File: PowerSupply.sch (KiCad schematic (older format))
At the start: 13 parts, among them IC1 TPS61240IDRVRQ1, U1 LM27762

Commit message: selecting actual components
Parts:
- removed C1: 4.7u/10V, symbol Device:C
- removed C2, C5, C6: 2.2u/16V, symbol Device:C
- removed C4: C, symbol Device:C
- removed IC1: TPS61240IDRVRQ1, SamacSys_PCB_Library:SON65P200X200X80-7N, symbol BalancedAudioBox:TPS61240IDRVRQ1
- removed L1: 1u/1.3A, symbol Device:L
- added C?: 100p, Capacitor_SMD:C_0201_0603Metric, symbol Device:C
- added C? (x5): 10u/25V, Resistor_SMD:R_0805_2012Metric, symbol Device:C
- added IC?: TPS61252DSGT, SON50P200X200X80-9N, symbol BalancedAudioBox:TPS61252DSGT
- added L?: 1.5u, symbol Device:L
- added R?: 634k, Resistor_SMD:R_0603_1608Metric, symbol Device:R
- added R?: 180k, Resistor_SMD:R_0603_1608Metric, symbol Device:R
- added R?: 47k, Resistor_SMD:R_0402_1005Metric, symbol Device:R
- R1, R2: value R -> 1.58M
- R3, R4: value R -> 499k
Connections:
- net labels added: VIN
- wire segments 61 -> 78
- no-connect marks 0 -> 1
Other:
- note added: "2.5V-5V to 5.40V @ 0.1A"
- note added: "5.3V-5.5V to 2x5V @ 75mA"
- note added: "R_inp_lim=10k/I_inp_lim"
- note added: "minimum 2.2uF on output; but we already have 2x10u on load.\nmin. load: 5mA"
- moved on the sheet: R1, R2, R3, R4

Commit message: work
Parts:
- added C21, C22: 4.7u, Capacitor_SMD:C_0805_2012Metric, symbol Device:C
- added PS1: DPU01L-15, SamacSys_PCB_Library:DPU01L15, symbol BalancedAudioBox:DPU01L-15
- C1, C20, C4, C5, C6: renamed from C?; footprint Resistor_SMD:R_0805_2012Metric -> Capacitor_SMD:C_0805_2012Metric
- C3: footprint (none) -> Capacitor_SMD:C_0805_2012Metric
- IC1: renamed from IC?; footprint SON50P200X200X80-9N -> SamacSys_PCB_Library:SON50P200X200X80-9N
- gave numbers to parts that had none: 5
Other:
- note added: "Alternative power supply"
- note added: "minimum 2.2uF on output; at 20uF we already have a lot of overshoot\nmin. load: 5mA"
- note removed: "minimum 2.2uF on output; but we already have 2x10u on load.\nmin. load: 5mA"
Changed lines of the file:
@@
 F 0 "C3" H 6765 4146 50  0000 L CNN
 F 1 "4.7u" H 6765 4055 50  0000 L CNN
-F 2 "" H 6688 3950 50  0001 C CNN
+F 2 "Capacitor_SMD:C_0805_2012Metric" H 6688 3950 50  0001 C CNN
 F 3 "~" H 6650 4100 50  0001 C CNN
 	1    6650 4100
@@
 	6850 3700 6850 3400
 $Comp
-L BalancedAudioBox:TPS61252DSGT IC?
+L BalancedAudioBox:TPS61252DSGT IC1
 U 1 1 5D3E64AD
 P 3700 3300
-F 0 "IC?" H 4300 3565 50  0000 C CNN
+F 0 "IC1" H 4300 3565 50  0000 C CNN
 F 1 "TPS61252DSGT" H 4300 3474 50  0000 C CNN
-F 2 "SON50P200X200X80-9N" H 4750 3400 50  0001 L CNN
+F 2 "SamacSys_PCB_Library:SON50P200X200X80-9N" H 4750 3400 50  0001 L CNN
 F 3 "http://www.ti.com/lit/ds/symlink/tps61252.pdf" H 4750 3300 50  0001 L CNN
 F 4 "TPS61252DSGT, DC-DC Converter, 1500mA Adjustable, 3  6.5 V, Step Up, 3.25 MHz, 8-Pin SON W" H 4750 3200 50  0001 L CNN "Description"
@@
 $EndComp
 $Comp
-L Device:C C?
+L Device:C C2
 U 1 1 5D3E7B90
 P 4250 3600
-F 0 "C?" H 4365 3646 50  0000 L CNN
+F 0 "C2" H 4365 3646 50  0000 L CNN
 F 1 "100p" H 4365 3555 50  0000 L CNN
 F 2 "Capacitor_SMD:C_0201_0603Metric" H 4288 3450 50  0001 C CNN
@@
 $EndComp
 $Comp
-L Device:R R?
+L Device:R R14
 U 1 1 5D3E88D9
 P 4650 3600
-F 0 "R?" H 4720 3646 50  0000 L CNN
+F 0 "R14" H 4720 3646 50  0000 L CNN
 F 1 "634k" H 4720 3555 50  0000 L CNN
 F 2 "Resistor_SMD:R_0603_1608Metric" V 4580 3600 50  0001 C CNN
@@
 $EndComp
 $Comp
-L Device:R R?
+L Device:R R15
 U 1 1 5D3E95C9
 P 4650 4100
-F 0 "R?" H 4720 4146 50  0000 L CNN
+F 0 "R15" H 4720 4146 50  0000 L CNN
 F 1 "180k" H 4720 4055 50  0000 L CNN
 F 2 "Resistor_SMD:R_0603_1608Metric" V 4580 4100 50  0001 C CNN
@@
 NoConn ~ 2500 3600
 $Comp
-L Device:L L?
+L Device:L L1
 U 1 1 5D3EB043
 P 2200 3400
-F 0 "L?" V 2000 3400 50  0000 C CNN
+F 0 "L1" V 2000 3400 50  0000 C CNN
 F 1 "1.5u" V 2100 3400 50  0000 C CNN
 F 2 "" H 2200 3400 50  0001 C CNN
@@
 Connection ~ 4650 3400
 $Comp
-L power:GND #PWR?
+L power:GND #PWR052
 U 1 1 5D3FC530
 P 4000 4700
-F 0 "#PWR?" H 4000 4450 50  0001 C CNN
+F 0 "#PWR052" H 4000 4450 50  0001 C CNN
 F 1 "GND" H 4005 4527 50  0000 C CNN
 F 2 "" H 4000 4700 50  0001 C CNN
@@
 $EndComp
 $Comp
-L Device:R R?
+L Device:R R13
 U 1 1 5D3FE154
 P 3700 4000
-F 0 "R?" H 3630 3954 50  0000 R CNN
+F 0 "R13" H 3630 3954 50  0000 R CNN
 F 1 "47k" H 3630 4045 50  0000 R CNN
 F 2 "Resistor_SMD:R_0402_1005Metric" V 3630 4000 50  0001 C CNN
@@
 	3700 3850 3700 3600
 $Comp
-L power:GND #PWR?
+L power:GND #PWR051
 U 1 1 5D40A0B6
 P 3700 4700
-F 0 "#PWR?" H 3700 4450 50  0001 C CNN
+F 0 "#PWR051" H 3700 4450 50  0001 C CNN
 F 1 "GND" H 3705 4527 50  0000 C CNN
 F 2 "" H 3700 4700 50  0001 C CNN
@@
 2.5V-5V to 5.40V @ 0.1A
 $Comp
-L Device:C C?
+L Device:C C1
 U 1 1 5D41488C
 P 1700 3950
-F 0 "C?" H 1815 3996 50  0000 L CNN
+F 0 "C1" H 1815 3996 50  0000 L CNN
 F 1 "10u/25V" H 1815 3905 50  0000 L CNN
-F 2 "Resistor_SMD:R_0805_2012Metric" H 1738 3800 50  0001 C CNN
+F 2 "Capacitor_SMD:C_0805_2012Metric" H 1738 3800 50  0001 C CNN
 F 3 "~" H 1700 3950 50  0001 C CNN
 F 4 "TMK212BBJ106MG-T" H 1700 3950 50  0001 C CNN "PN"
@@
 $EndComp
 $Comp
-L Device:C C?
+L Device:C C4
 U 1 1 5D4150B1
 P 4950 3900
-F 0 "C?" H 5065 3946 50  0000 L CNN
+F 0 "C4" H 5065 3946 50  0000 L CNN
 F 1 "10u/25V" H 5065 3855 50  0000 L CNN
-F 2 "Resistor_SMD:R_0805_2012Metric" H 4988 3750 50  0001 C CNN
+F 2 "Capacitor_SMD:C_0805_2012Metric" H 4988 3750 50  0001 C CNN
 F 3 "~" H 4950 3900 50  0001 C CNN
 F 4 "TMK212BBJ106MG-T" H 4950 3900 50  0001 C CNN "PN"
@@
 $EndComp
 $Comp
-L power:GND #PWR?
+L power:GND #PWR053
 U 1 1 5D4185FE
 P 5500 4700
-F 0 "#PWR?" H 5500 4450 50  0001 C CNN
+F 0 "#PWR053" H 5500 4450 50  0001 C CNN
 F 1 "GND" H 5505 4527 50  0000 C CNN
 F 2 "" H 5500 4700 50  0001 C CNN
@@
 $EndComp
 $Comp
-L Device:C C?
+L Device:C C5
 U 1 1 5D418607
 P 5500 3900
-F 0 "C?" H 5615 3946 50  0000 L CNN
+F 0 "C5" H 5615 3946 50  0000 L CNN
 F 1 "10u/25V" H 5615 3855 50  0000 L CNN
-F 2 "Resistor_SMD:R_0805_2012Metric" H 5538 3750 50  0001 C CNN
+F 2 "Capacitor_SMD:C_0805_2012Metric" H 5538 3750 50  0001 C CNN
 F 3 "~" H 5500 3900 50  0001 C CNN
 F 4 "TMK212BBJ106MG-T" H 5500 3900 50  0001 C CNN "PN"
@@
 $EndComp
 $Comp
-L power:GND #PWR?
+L power:GND #PWR054
 U 1 1 5D41A9F0
 P 6050 4700
-F 0 "#PWR?" H 6050 4450 50  0001 C CNN
+F 0 "#PWR054" H 6050 4450 50  0001 C CNN
 F 1 "GND" H 6055 4527 50  0000 C CNN
 F 2 "" H 6050 4700 50  0001 C CNN
@@
 $EndComp
 $Comp
-L Device:C C?
+L Device:C C6
 U 1 1 5D41A9F9
 P 6050 3900
-F 0 "C?" H 6165 3946 50  0000 L CNN
+F 0 "C6" H 6165 3946 50  0000 L CNN
 F 1 "10u/25V" H 6165 3855 50  0000 L CNN
-F 2 "Resistor_SMD:R_0805_2012Metric" H 6088 3750 50  0001 C CNN
+F 2 "Capacitor_SMD:C_0805_2012Metric" H 6088 3750 50  0001 C CNN
 F 3 "~" H 6050 3900 50  0001 C CNN
 F 4 "TMK212BBJ106MG-T" H 6050 3900 50  0001 C CNN "PN"
@@
 	1700 3300 1900 3300
 $Comp
-L power:GND #PWR?
+L power:GND #PWR050
 U 1 1 5D43E999
 P 1700 4700
-F 0 "#PWR?" H 1700 4450 50  0001 C CNN
+F 0 "#PWR050" H 1700 4450 50  0001 C CNN
 F 1 "GND" H 1705 4527 50  0000 C CNN
 F 2 "" H 1700 4700 50  0001 C CNN
@@
 Connection ~ 10550 4350
 $Comp
-L Device:C C?
+L Device:C C20
 U 1 1 5D45C51D
 P 8100 4500
-F 0 "C?" H 8215 4546 50  0000 L CNN
+F 0 "C20" H 8215 4546 50  0000 L CNN
 F 1 "10u/25V" H 8215 4455 50  0000 L CNN
-F 2 "Resistor_SMD:R_0805_2012Metric" H 8138 4350 50  0001 C CNN
+F 2 "Capacitor_SMD:C_0805_2012Metric" H 8138 4350 50  0001 C CNN
 F 3 "~" H 8100 4500 50  0001 C CNN
 F 4 "TMK212BBJ106MG-T" H 8100 4500 50  0001 C CNN "PN"
@@
 	4000 3300 4000 4700
 Text Notes 8150 5400 0    50   ~ 0
-minimum 2.2uF on output; but we already have 2x10u on load.\nmin. load: 5mA
+minimum 2.2uF on output; at 20uF we already have a lot of overshoot\nmin. load: 5mA
+$Comp
+L BalancedAudioBox:DPU01L-15 PS1
+U 1 1 5D3EF611
+P 4600 1650
+F 0 "PS1" H 5250 1915 50  0000 C CNN
+F 1 "DPU01L-15" H 5250 1824 50  0000 C CNN
+F 2 "SamacSys_PCB_Library:DPU01L15" H 5750 1750 50  0001 L CNN
+F 3 "https://media.digikey.com/pdf/Data%20Sheets/Mean%20Well%20PDF's/SPU01,DUP01_Series_Ds.pdf" H 5750 1650 50  0001 L CNN
+F 4 "Isolated DC/DC Converters 4.5-5.5Vin +/-15Vout +/-33mA SIP6 Unreg" H 5750 1550 50  0001 L CNN "Description"
+F 5 "10.45" H 5750 1450 50  0001 L CNN "Height"
+F 6 "Mean Well" H 5750 1350 50  0001 L CNN "Manufacturer_Name"
+F 7 "DPU01L-15" H 5750 1250 50  0001 L CNN "Manufacturer_Part_Number"
+F 8 "709-DPU01L-15" H 5750 1150 50  0001 L CNN "Mouser Part Number"
+F 9 "https://www.mouser.com/Search/Refine.aspx?Keyword=709-DPU01L-15" H 5750 1050 50  0001 L CNN "Mouser Price/Stock"
+F 10 "" H 5750 950 50  0001 L CNN "RS Part Number"
+F 11 "" H 5750 850 50  0001 L CNN "RS Price/Stock"
+F 12 "71028144" H 5750 750 50  0001 L CNN "Allied_Number"
+F 13 "https://www.alliedelec.com/meanwellusa-dpu01l-15/71028144/" H 5750 650 50  0001 L CNN "Allied Price/Stock"
+	1    4600 1650
+	1    0    0    -1
+$EndComp
+Text Notes 4900 1200 0    50   ~ 0
+Alternative power supply
+$Comp
+L Device:C C21
+U 1 1 5D3F13AC
+P 8650 4500
+F 0 "C21" H 8765 4546 50  0000 L CNN
+F 1 "4.7u" H 8765 4455 50  0000 L CNN
+F 2 "Capacitor_SMD:C_0805_2012Metric" H 8688 4350 50  0001 C CNN
+F 3 "~" H 8650 4500 50  0001 C CNN
+	1    8650 4500
+	1    0    0    -1
+$EndComp
+$Comp
+L Device:C C22
+U 1 1 5D3F1A6F
+P 9300 4500
+F 0 "C22" H 9415 4546 50  0000 L CNN
+F 1 "4.7u" H 9415 4455 50  0000 L CNN
+F 2 "Capacitor_SMD:C_0805_2012Metric" H 9338 4350 50  0001 C CNN
+F 3 "~" H 9300 4500 50  0001 C CNN
+	1    9300 4500
+	1    0    0    -1
+$EndComp
 $EndSCHEMATC

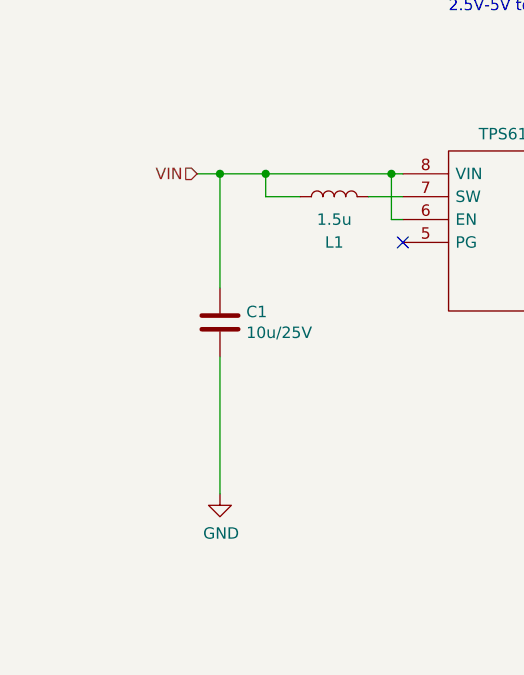
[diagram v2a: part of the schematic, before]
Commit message: TPS61252 done
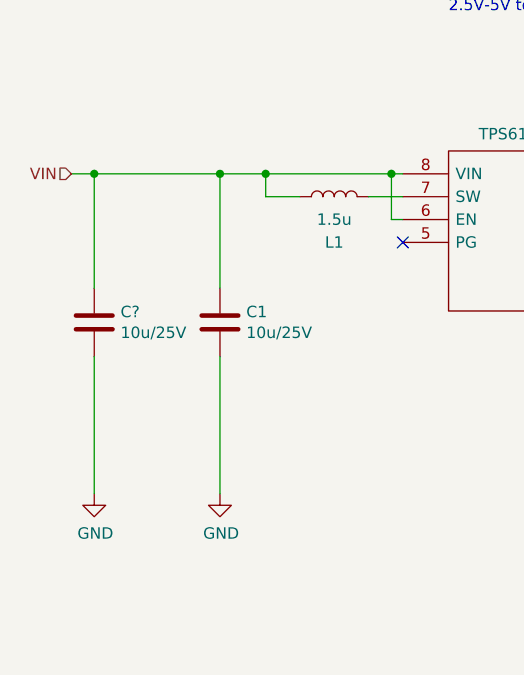
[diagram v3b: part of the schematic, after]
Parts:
- added C?: 10u/25V, Capacitor_SMD:C_0805_2012Metric, symbol Device:C
- C2: footprint Capacitor_SMD:C_0201_0603Metric -> Capacitor_SMD:C_0603_1608Metric
- L1: footprint (none) -> BalancedAudioBox:SRN30151R5Y
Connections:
- net GND: now also C?.2
- net VIN: now also C?.1
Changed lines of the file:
@@
 F 0 "C2" H 4365 3646 50  0000 L CNN
 F 1 "100p" H 4365 3555 50  0000 L CNN
-F 2 "Capacitor_SMD:C_0201_0603Metric" H 4288 3450 50  0001 C CNN
+F 2 "Capacitor_SMD:C_0603_1608Metric" H 4288 3450 50  0001 C CNN
 F 3 "~" H 4250 3600 50  0001 C CNN
 F 4 "GRM1885C2A101JA01D" H 4250 3600 50  0001 C CNN "PN"
@@
 F 0 "L1" V 2000 3400 50  0000 C CNN
 F 1 "1.5u" V 2100 3400 50  0000 C CNN
-F 2 "" H 2200 3400 50  0001 C CNN
+F 2 "BalancedAudioBox:SRN30151R5Y" H 2200 3400 50  0001 C CNN
 F 3 "~" H 2200 3400 50  0001 C CNN
 F 4 "SRN3015-1R5Y" V 2200 3400 50  0001 C CNN "PN"
@@
 Text Notes 3350 5200 0    50   ~ 0
 R_inp_lim=10k/I_inp_lim
-Text HLabel 1600 3300 0    50   Input ~ 0
+Text HLabel 1050 3300 0    50   Input ~ 0
 VIN
-Wire Wire Line
-	1600 3300 1700 3300
 Connection ~ 1900 3300
 Text Notes 2700 2600 0    50   ~ 0
@@
 	1    0    0    -1
 $EndComp
+Wire Wire Line
+	1050 3300 1150 3300
+$Comp
+L Device:C C?
+U 1 1 5D43E98B
+P 1150 3950
+F 0 "C?" H 1265 3996 50  0000 L CNN
+F 1 "10u/25V" H 1265 3905 50  0000 L CNN
+F 2 "Capacitor_SMD:C_0805_2012Metric" H 1188 3800 50  0001 C CNN
+F 3 "~" H 1150 3950 50  0001 C CNN
+F 4 "TMK212BBJ106MG-T" H 1150 3950 50  0001 C CNN "PN"
+	1    1150 3950
+	1    0    0    -1
+$EndComp
+Wire Wire Line
+	1150 3800 1150 3300
+$Comp
+L power:GND #PWR?
+U 1 1 5D43E992
+P 1150 4700
+F 0 "#PWR?" H 1150 4450 50  0001 C CNN
+F 1 "GND" H 1155 4527 50  0000 C CNN
+F 2 "" H 1150 4700 50  0001 C CNN
+F 3 "" H 1150 4700 50  0001 C CNN
+	1    1150 4700
+	1    0    0    -1
+$EndComp
+Wire Wire Line
+	1150 4700 1150 4100
+Connection ~ 1150 3300
+Wire Wire Line
+	1150 3300 1700 3300
 $EndSCHEMATC

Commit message: ps checked
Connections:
- net +5V: now also PS1.6 (+VOUT)
- net -5V: now also PS1.4 (-VOUT)
- net GND: now also PS1.2 (-VIN), PS1.5 (COMMON)
- net VIN: now also PS1.1 (+VIN)
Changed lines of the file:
@@
 Wire Wire Line
 	1150 3300 1700 3300
+$Comp
+L power:+5V #PWR?
+U 1 1 5D43903A
+P 6100 1500
+F 0 "#PWR?" H 6100 1350 50  0001 C CNN
+F 1 "+5V" H 6115 1673 50  0000 C CNN
+F 2 "" H 6100 1500 50  0001 C CNN
+F 3 "" H 6100 1500 50  0001 C CNN
+	1    6100 1500
+	1    0    0    -1
+$EndComp
+$Comp
+L power:-5V #PWR?
+U 1 1 5D4393F5
+P 4500 2000
+F 0 "#PWR?" H 4500 2100 50  0001 C CNN
+F 1 "-5V" H 4515 2173 50  0000 C CNN
+F 2 "" H 4500 2000 50  0001 C CNN
+F 3 "" H 4500 2000 50  0001 C CNN
+	1    4500 2000
+	-1   0    0    1
+$EndComp
+$Comp
+L power:GND #PWR?
+U 1 1 5D439932
+P 5950 2050
+F 0 "#PWR?" H 5950 1800 50  0001 C CNN
+F 1 "GND" H 5955 1877 50  0000 C CNN
+F 2 "" H 5950 2050 50  0001 C CNN
+F 3 "" H 5950 2050 50  0001 C CNN
+	1    5950 2050
+	1    0    0    -1
+$EndComp
+Text Label 1700 3300 0    50   ~ 0
+VIN
+Text Label 4300 1650 0    50   ~ 0
+VIN
+Wire Wire Line
+	4600 1650 4300 1650
+$Comp
+L power:GND #PWR?
+U 1 1 5D43C58F
+P 4100 2000
+F 0 "#PWR?" H 4100 1750 50  0001 C CNN
+F 1 "GND" H 4105 1827 50  0000 C CNN
+F 2 "" H 4100 2000 50  0001 C CNN
+F 3 "" H 4100 2000 50  0001 C CNN
+	1    4100 2000
+	1    0    0    -1
+$EndComp
+Wire Wire Line
+	4100 2000 4100 1750
+Wire Wire Line
+	4100 1750 4600 1750
+Wire Wire Line
+	4600 1850 4500 1850
+Wire Wire Line
+	4500 1850 4500 2000
+Wire Wire Line
+	5900 1750 6100 1750
+Wire Wire Line
+	6100 1750 6100 1500
+Wire Wire Line
+	5950 2050 5950 1650
+Wire Wire Line
+	5950 1650 5900 1650
 $EndSCHEMATC

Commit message: placement complete
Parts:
- added J6: Conn_01x02, Connector_PinSocket_2.54mm:PinSocket_1x02_P2.54mm_Vertical, symbol Connector_Generic:Conn_01x02
- IC1: footprint SamacSys_PCB_Library:SON50P200X200X80-9N -> BalancedAudioBox:SON50P200X200X80-9N
- PS1: footprint SamacSys_PCB_Library:DPU01L15 -> BalancedAudioBox:DPU01L15
- gave numbers to parts that had none: 1
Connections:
- net GND: now also J6.2 (Pin_2)
- net VOUT-5.4V: now reaches C2.1, C4.1, C5.1, C6.1, IC1.2 (VOUT), R14.1, U1.12 (EN+), U1.3 (VIN), U1.8 (EN-)
- net VOUT-5.4V: now also J6.1 (Pin_1)
- net FB: now reaches C2.2, IC1.3 (FB), R14.2, R15.1
- net ILIM: now reaches IC1.4 (ILIM), R13.2
- net FB+: now reaches R1.2, R4.1, U1.2 (FB+)
- net CP: now reaches C20.1, U1.5 (CP)
- net FB-: now reaches R2.2, R3.1, U1.7 (FB-)
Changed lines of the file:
@@
 F 0 "IC1" H 4300 3565 50  0000 C CNN
 F 1 "TPS61252DSGT" H 4300 3474 50  0000 C CNN
-F 2 "SamacSys_PCB_Library:SON50P200X200X80-9N" H 4750 3400 50  0001 L CNN
+F 2 "BalancedAudioBox:SON50P200X200X80-9N" H 4750 3400 50  0001 L CNN
 F 3 "http://www.ti.com/lit/ds/symlink/tps61252.pdf" H 4750 3300 50  0001 L CNN
 F 4 "TPS61252DSGT, DC-DC Converter, 1500mA Adjustable, 3  6.5 V, Step Up, 3.25 MHz, 8-Pin SON W" H 4750 3200 50  0001 L CNN "Description"
@@
 Connection ~ 4950 3400
 Wire Wire Line
-	4950 3400 5500 3400
+	4950 3400 5150 3400
 Wire Wire Line
 	5500 3750 5500 3400
@@
 F 0 "PS1" H 5250 1915 50  0000 C CNN
 F 1 "DPU01L-15" H 5250 1824 50  0000 C CNN
-F 2 "SamacSys_PCB_Library:DPU01L15" H 5750 1750 50  0001 L CNN
+F 2 "BalancedAudioBox:DPU01L15" H 5750 1750 50  0001 L CNN
 F 3 "https://media.digikey.com/pdf/Data%20Sheets/Mean%20Well%20PDF's/SPU01,DUP01_Series_Ds.pdf" H 5750 1650 50  0001 L CNN
 F 4 "Isolated DC/DC Converters 4.5-5.5Vin +/-15Vout +/-33mA SIP6 Unreg" H 5750 1550 50  0001 L CNN "Description"
@@
 	1050 3300 1150 3300
 $Comp
-L Device:C C?
+L Device:C C27
 U 1 1 5D43E98B
 P 1150 3950
-F 0 "C?" H 1265 3996 50  0000 L CNN
+F 0 "C27" H 1265 3996 50  0000 L CNN
 F 1 "10u/25V" H 1265 3905 50  0000 L CNN
 F 2 "Capacitor_SMD:C_0805_2012Metric" H 1188 3800 50  0001 C CNN
@@
 	1150 3800 1150 3300
 $Comp
-L power:GND #PWR?
+L power:GND #PWR072
 U 1 1 5D43E992
 P 1150 4700
-F 0 "#PWR?" H 1150 4450 50  0001 C CNN
+F 0 "#PWR072" H 1150 4450 50  0001 C CNN
 F 1 "GND" H 1155 4527 50  0000 C CNN
 F 2 "" H 1150 4700 50  0001 C CNN
@@
 	1150 3300 1700 3300
 $Comp
-L power:+5V #PWR?
+L power:+5V #PWR076
 U 1 1 5D43903A
 P 6100 1500
-F 0 "#PWR?" H 6100 1350 50  0001 C CNN
+F 0 "#PWR076" H 6100 1350 50  0001 C CNN
 F 1 "+5V" H 6115 1673 50  0000 C CNN
 F 2 "" H 6100 1500 50  0001 C CNN
@@
 $EndComp
 $Comp
-L power:-5V #PWR?
+L power:-5V #PWR074
 U 1 1 5D4393F5
 P 4500 2000
-F 0 "#PWR?" H 4500 2100 50  0001 C CNN
+F 0 "#PWR074" H 4500 2100 50  0001 C CNN
 F 1 "-5V" H 4515 2173 50  0000 C CNN
 F 2 "" H 4500 2000 50  0001 C CNN
@@
 $EndComp
 $Comp
-L power:GND #PWR?
+L power:GND #PWR075
 U 1 1 5D439932
 P 5950 2050
-F 0 "#PWR?" H 5950 1800 50  0001 C CNN
+F 0 "#PWR075" H 5950 1800 50  0001 C CNN
 F 1 "GND" H 5955 1877 50  0000 C CNN
 F 2 "" H 5950 2050 50  0001 C CNN
@@
 	4600 1650 4300 1650
 $Comp
-L power:GND #PWR?
+L power:GND #PWR073
 U 1 1 5D43C58F
 P 4100 2000
-F 0 "#PWR?" H 4100 1750 50  0001 C CNN
+F 0 "#PWR073" H 4100 1750 50  0001 C CNN
 F 1 "GND" H 4105 1827 50  0000 C CNN
 F 2 "" H 4100 2000 50  0001 C CNN
@@
 Wire Wire Line
 	5950 1650 5900 1650
+$Comp
+L Connector_Generic:Conn_01x02 J6
+U 1 1 5D46B0BF
+P 5500 3050
+F 0 "J6" H 5580 3042 50  0000 L CNN
+F 1 "Conn_01x02" H 5580 2951 50  0000 L CNN
+F 2 "Connector_PinSocket_2.54mm:PinSocket_1x02_P2.54mm_Vertical" H 5500 3050 50  0001 C CNN
+F 3 "~" H 5500 3050 50  0001 C CNN
+	1    5500 3050
+	1    0    0    -1
+$EndComp
+$Comp
+L power:GND #PWR077
+U 1 1 5D46C0AE
+P 5300 3150
+F 0 "#PWR077" H 5300 2900 50  0001 C CNN
+F 1 "GND" H 5305 2977 50  0000 C CNN
+F 2 "" H 5300 3150 50  0001 C CNN
+F 3 "" H 5300 3150 50  0001 C CNN
+	1    5300 3150
+	1    0    0    -1
+$EndComp
+Wire Wire Line
+	5300 3050 5150 3050
+Wire Wire Line
+	5150 3050 5150 3400
+Connection ~ 5150 3400
+Wire Wire Line
+	5150 3400 5500 3400
+Text Label 6050 3400 0    50   ~ 0
+VOUT-5.4V
+Text Label 8100 4200 0    50   ~ 0
+CP
+Text Label 8100 4000 0    50   ~ 0
+OUT-
+Text Label 8100 3800 0    50   ~ 0
+FB-
+Text Label 8100 3600 0    50   ~ 0
+FB+
+Text Label 6500 3600 0    50   ~ 0
+PGOOD
+Text Label 3700 3600 0    50   ~ 0
+ILIM
+Text Label 4250 3850 0    50   ~ 0
+FB
 $EndSCHEMATC

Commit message: footprint and 3d improvements
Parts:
- R1, R14, R15, R2, R3, R4: footprint Resistor_SMD:R_0603_1608Metric -> Resistor_SMD:R_0402_1005Metric
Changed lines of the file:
@@
 F 0 "R3" H 9920 4596 50  0000 L CNN
 F 1 "499k" H 9920 4505 50  0000 L CNN
-F 2 "Resistor_SMD:R_0603_1608Metric" V 9780 4550 50  0001 C CNN
+F 2 "Resistor_SMD:R_0402_1005Metric" V 9780 4550 50  0001 C CNN
 F 3 "~" H 9850 4550 50  0001 C CNN
 	1    9850 4550
@@
 F 0 "R2" H 9920 4246 50  0000 L CNN
 F 1 "1.58M" H 9920 4155 50  0000 L CNN
-F 2 "Resistor_SMD:R_0603_1608Metric" V 9780 4200 50  0001 C CNN
+F 2 "Resistor_SMD:R_0402_1005Metric" V 9780 4200 50  0001 C CNN
 F 3 "~" H 9850 4200 50  0001 C CNN
 	1    9850 4200
@@
 F 0 "R4" H 10620 4596 50  0000 L CNN
 F 1 "499k" H 10620 4505 50  0000 L CNN
-F 2 "Resistor_SMD:R_0603_1608Metric" V 10480 4550 50  0001 C CNN
+F 2 "Resistor_SMD:R_0402_1005Metric" V 10480 4550 50  0001 C CNN
 F 3 "~" H 10550 4550 50  0001 C CNN
 	1    10550 4550
@@
 F 0 "R1" H 10620 4246 50  0000 L CNN
 F 1 "1.58M" H 10620 4155 50  0000 L CNN
-F 2 "Resistor_SMD:R_0603_1608Metric" V 10480 4200 50  0001 C CNN
+F 2 "Resistor_SMD:R_0402_1005Metric" V 10480 4200 50  0001 C CNN
 F 3 "~" H 10550 4200 50  0001 C CNN
 	1    10550 4200
@@
 F 0 "R14" H 4720 3646 50  0000 L CNN
 F 1 "634k" H 4720 3555 50  0000 L CNN
-F 2 "Resistor_SMD:R_0603_1608Metric" V 4580 3600 50  0001 C CNN
+F 2 "Resistor_SMD:R_0402_1005Metric" V 4580 3600 50  0001 C CNN
 F 3 "~" H 4650 3600 50  0001 C CNN
 	1    4650 3600
@@
 F 0 "R15" H 4720 4146 50  0000 L CNN
 F 1 "180k" H 4720 4055 50  0000 L CNN
-F 2 "Resistor_SMD:R_0603_1608Metric" V 4580 4100 50  0001 C CNN
+F 2 "Resistor_SMD:R_0402_1005Metric" V 4580 4100 50  0001 C CNN
 F 3 "~" H 4650 4100 50  0001 C CNN
 	1    4650 4100

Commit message: layout and silk
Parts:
- J6: footprint Connector_PinSocket_2.54mm:PinSocket_1x02_P2.54mm_Vertical -> Connector_PinHeader_2.54mm:PinHeader_1x02_P2.54mm_Vertical
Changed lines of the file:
@@
 F 0 "J6" H 5580 3042 50  0000 L CNN
 F 1 "Conn_01x02" H 5580 2951 50  0000 L CNN
-F 2 "Connector_PinSocket_2.54mm:PinSocket_1x02_P2.54mm_Vertical" H 5500 3050 50  0001 C CNN
+F 2 "Connector_PinHeader_2.54mm:PinHeader_1x02_P2.54mm_Vertical" H 5500 3050 50  0001 C CNN
 F 3 "~" H 5500 3050 50  0001 C CNN
 	1    5500 3050

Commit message: more layout
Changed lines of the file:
@@
 Wire Wire Line
 	5150 3400 5500 3400
-Text Label 6050 3400 0    50   ~ 0
-VOUT-5.4V
 Text Label 8100 4200 0    50   ~ 0
 CP
@@
 Text Label 4250 3850 0    50   ~ 0
 FB
+Text GLabel 5350 2800 2    50   Input ~ 0
+VOUT-5.4V
+Wire Wire Line
+	5150 3050 5150 2800
+Wire Wire Line
+	5150 2800 5350 2800
+Connection ~ 5150 3050
 $EndSCHEMATC
